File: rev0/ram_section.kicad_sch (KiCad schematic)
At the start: 2 parts, among them IC1 ECP5-BGA256, U10 HyperRAM

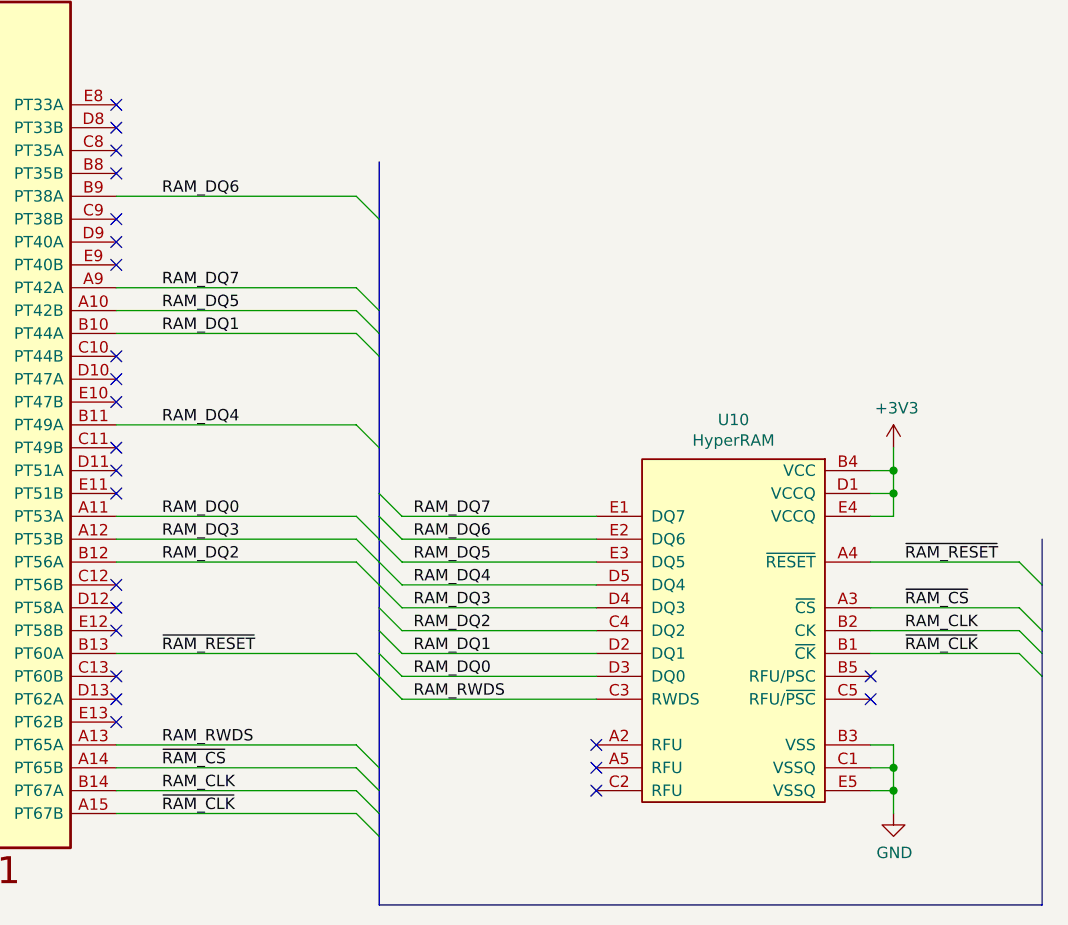
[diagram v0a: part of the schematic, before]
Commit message: hardware: rename buses for KiCad 6
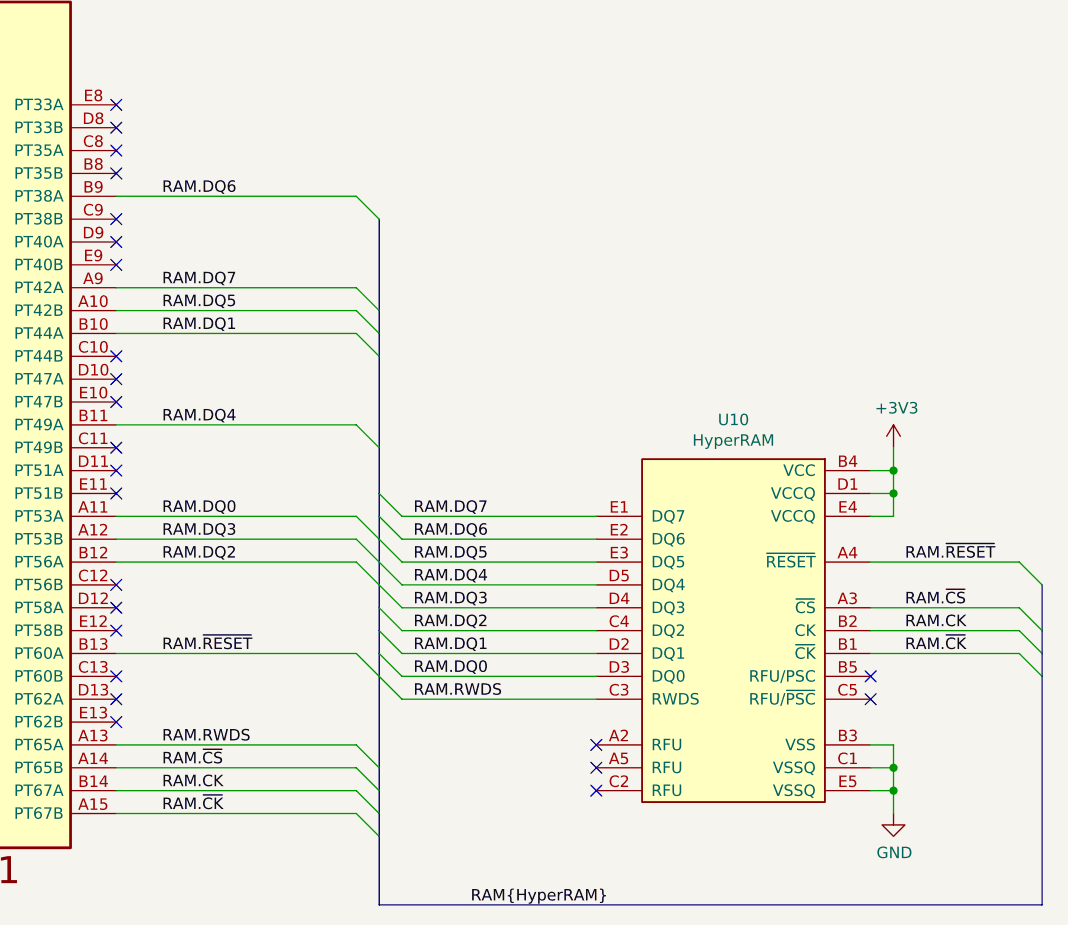
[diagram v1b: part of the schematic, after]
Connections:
- net RAM_CLK renamed RAM.CK
- net RAM_DQ0 renamed RAM.DQ0
- net RAM_DQ1 renamed RAM.DQ1
- net RAM_DQ2 renamed RAM.DQ2
- net RAM_DQ3 renamed RAM.DQ3
- net RAM_DQ4 renamed RAM.DQ4
- net RAM_DQ5 renamed RAM.DQ5
- net RAM_DQ6 renamed RAM.DQ6
- net RAM_DQ7 renamed RAM.DQ7
- net RAM_RWDS renamed RAM.RWDS
- net ~{RAM_CLK} renamed RAM.~{CK}
- net ~{RAM_CS} renamed RAM.~{CS}
- net ~{RAM_RESET} renamed RAM.~{RESET}
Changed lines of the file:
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@@
     (comment 1 "Licensed under the CERN-OHL-P v2")
   )
+  (bus_alias "HyperRAM" (members "DQ[0..7]" "CK" "~{CK}" "~{CS}" "RWDS" "~{RESET}"))
   (junction (at 154.94 138.43) (diameter 0) (color 0 0 0 0)
   )
@@
     (stroke (width 0) (type default) (color 0 0 0 0))
   )
-  (bus (pts (xy 171.45 113.03) (xy 171.45 118.11))
-    (stroke (width 0) (type default) (color 0 0 0 0))
-  )
   (wire (pts (xy 68.58 140.97) (xy 95.25 140.97))
     (stroke (width 0) (type default) (color 0 0 0 0))
@@
     (stroke (width 0) (type default) (color 0 0 0 0))
   )
-  (bus (pts (xy 97.79 71.12) (xy 97.79 77.47))
-    (stroke (width 0) (type default) (color 0 0 0 0))
-  )
   (wire (pts (xy 68.58 138.43) (xy 95.25 138.43))
     (stroke (width 0) (type default) (color 0 0 0 0))
@@
     (stroke (width 0) (type default) (color 0 0 0 0))
   )
-  (label "RAM_DQ6" (at 73.66 74.93 0)
-    (effects (font (size 1.27 1.27)) (justify left bottom))
-  )
-  (label "RAM_DQ3" (at 101.6 120.65 0)
-    (effects (font (size 1.27 1.27)) (justify left bottom))
-  )
-  (label "RAM_DQ4" (at 101.6 118.11 0)
-    (effects (font (size 1.27 1.27)) (justify left bottom))
-  )
-  (label "RAM_DQ2" (at 73.66 115.57 0)
-    (effects (font (size 1.27 1.27)) (justify left bottom))
-  )
-  (label "RAM_DQ7" (at 73.66 85.09 0)
-    (effects (font (size 1.27 1.27)) (justify left bottom))
-  )
-  (label "~{RAM_RESET}" (at 73.66 125.73 0)
-    (effects (font (size 1.27 1.27)) (justify left bottom))
-  )
-  (label "RAM_DQ0" (at 73.66 110.49 0)
-    (effects (font (size 1.27 1.27)) (justify left bottom))
-  )
-  (label "RAM_DQ5" (at 101.6 115.57 0)
-    (effects (font (size 1.27 1.27)) (justify left bottom))
-  )
-  (label "RAM_DQ0" (at 101.6 128.27 0)
-    (effects (font (size 1.27 1.27)) (justify left bottom))
-  )
-  (label "RAM_DQ6" (at 101.6 113.03 0)
-    (effects (font (size 1.27 1.27)) (justify left bottom))
-  )
-  (label "~{RAM_CS}" (at 156.21 120.65 0)
-    (effects (font (size 1.27 1.27)) (justify left bottom))
-  )
-  (label "~{RAM_RESET}" (at 156.21 115.57 0)
-    (effects (font (size 1.27 1.27)) (justify left bottom))
-  )
-  (label "~{RAM_CS}" (at 73.66 138.43 0)
-    (effects (font (size 1.27 1.27)) (justify left bottom))
-  )
-  (label "RAM_DQ3" (at 73.66 113.03 0)
-    (effects (font (size 1.27 1.27)) (justify left bottom))
-  )
-  (label "RAM_RWDS" (at 101.6 130.81 0)
-    (effects (font (size 1.27 1.27)) (justify left bottom))
-  )
-  (label "RAM_CLK" (at 156.21 123.19 0)
-    (effects (font (size 1.27 1.27)) (justify left bottom))
-  )
-  (label "RAM_DQ1" (at 73.66 90.17 0)
-    (effects (font (size 1.27 1.27)) (justify left bottom))
-  )
-  (label "RAM_CLK" (at 73.66 140.97 0)
-    (effects (font (size 1.27 1.27)) (justify left bottom))
-  )
-  (label "~{RAM_CLK}" (at 156.21 125.73 0)
-    (effects (font (size 1.27 1.27)) (justify left bottom))
-  )
-  (label "RAM_DQ7" (at 101.6 110.49 0)
-    (effects (font (size 1.27 1.27)) (justify left bottom))
-  )
-  (label "RAM_DQ2" (at 101.6 123.19 0)
-    (effects (font (size 1.27 1.27)) (justify left bottom))
-  )
-  (label "RAM_DQ5" (at 73.66 87.63 0)
-    (effects (font (size 1.27 1.27)) (justify left bottom))
-  )
-  (label "RAM_RWDS" (at 73.66 135.89 0)
-    (effects (font (size 1.27 1.27)) (justify left bottom))
-  )
-  (label "RAM_DQ1" (at 101.6 125.73 0)
-    (effects (font (size 1.27 1.27)) (justify left bottom))
-  )
-  (label "~{RAM_CLK}" (at 73.66 143.51 0)
-    (effects (font (size 1.27 1.27)) (justify left bottom))
-  )
-  (label "RAM_DQ4" (at 73.66 100.33 0)
-    (effects (font (size 1.27 1.27)) (justify left bottom))
-  )
+  (label "RAM.DQ6" (at 73.66 74.93 0)
+    (effects (font (size 1.27 1.27)) (justify left bottom))
+  )
+  (label "RAM.DQ3" (at 101.6 120.65 0)
+    (effects (font (size 1.27 1.27)) (justify left bottom))
+  )
+  (label "RAM.DQ4" (at 101.6 118.11 0)
+    (effects (font (size 1.27 1.27)) (justify left bottom))
+  )
+  (label "RAM.DQ2" (at 73.66 115.57 0)
+    (effects (font (size 1.27 1.27)) (justify left bottom))
+  )
+  (label "RAM.DQ7" (at 73.66 85.09 0)
+    (effects (font (size 1.27 1.27)) (justify left bottom))
+  )
+  (label "RAM.~{RESET}" (at 73.66 125.73 0)
+    (effects (font (size 1.27 1.27)) (justify left bottom))
+  )
+  (label "RAM.DQ0" (at 73.66 110.49 0)
+    (effects (font (size 1.27 1.27)) (justify left bottom))
+  )
+  (label "RAM.DQ5" (at 101.6 115.57 0)
+    (effects (font (size 1.27 1.27)) (justify left bottom))
+  )
+  (label "RAM.DQ0" (at 101.6 128.27 0)
+    (effects (font (size 1.27 1.27)) (justify left bottom))
+  )
+  (label "RAM.DQ6" (at 101.6 113.03 0)
+    (effects (font (size 1.27 1.27)) (justify left bottom))
+  )
+  (label "RAM.~{CS}" (at 156.21 120.65 0)
+    (effects (font (size 1.27 1.27)) (justify left bottom))
+  )
+  (label "RAM.~{RESET}" (at 156.21 115.57 0)
+    (effects (font (size 1.27 1.27)) (justify left bottom))
+  )
+  (label "RAM{HyperRAM}" (at 107.95 153.67 0)
+    (effects (font (size 1.27 1.27)) (justify left bottom))
+  )
+  (label "RAM.~{CS}" (at 73.66 138.43 0)
+    (effects (font (size 1.27 1.27)) (justify left bottom))
+  )
+  (label "RAM.DQ3" (at 73.66 113.03 0)
+    (effects (font (size 1.27 1.27)) (justify left bottom))
+  )
+  (label "RAM.RWDS" (at 101.6 130.81 0)
+    (effects (font (size 1.27 1.27)) (justify left bottom))
+  )
+  (label "RAM.CK" (at 156.21 123.19 0)
+    (effects (font (size 1.27 1.27)) (justify left bottom))
+  )
+  (label "RAM.DQ1" (at 73.66 90.17 0)
+    (effects (font (size 1.27 1.27)) (justify left bottom))
+  )
+  (label "RAM.CK" (at 73.66 140.97 0)
+    (effects (font (size 1.27 1.27)) (justify left bottom))
+  )
+  (label "RAM.~{CK}" (at 156.21 125.73 0)
+    (effects (font (size 1.27 1.27)) (justify left bottom))
+  )
+  (label "RAM.DQ7" (at 101.6 110.49 0)
+    (effects (font (size 1.27 1.27)) (justify left bottom))
+  )
+  (label "RAM.DQ2" (at 101.6 123.19 0)
+    (effects (font (size 1.27 1.27)) (justify left bottom))
+  )
+  (label "RAM.DQ5" (at 73.66 87.63 0)
+    (effects (font (size 1.27 1.27)) (justify left bottom))
+  )
+  (label "RAM.RWDS" (at 73.66 135.89 0)
+    (effects (font (size 1.27 1.27)) (justify left bottom))
+  )
+  (label "RAM.DQ1" (at 101.6 125.73 0)
+    (effects (font (size 1.27 1.27)) (justify left bottom))
+  )
+  (label "RAM.~{CK}" (at 73.66 143.51 0)
+    (effects (font (size 1.27 1.27)) (justify left bottom))
+  )
+  (label "RAM.DQ4" (at 73.66 100.33 0)
+    (effects (font (size 1.27 1.27)) (justify left bottom))
+  )
